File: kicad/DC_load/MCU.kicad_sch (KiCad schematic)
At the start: 125 parts, among them J1 BNC, J10 DC fan connector, J6 USB_B, J8 FT232 programming port, J9 Conn_01x04_Socket, Q1 MMBT5401, Q13 AO3400A, SW1 RotaryEncoder_Switch, SW2 RotaryEncoder_Switch, SW3 SW_Push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

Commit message: Added jumper.
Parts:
- added JP3: Jumper_2_Open, Jumper:SolderJumper-2_P1.3mm_Open_RoundedPad1.0x1.5mm, symbol Jumper:Jumper_2_Open
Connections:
- net CH1_CONTROL: now also JP3.2 (B)
- net at C22.2, R21.1, U1.3: now also JP3.1 (A)
- no-connect marks 16 -> 17
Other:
- note added: "Analog switch supply"
- note added: "Fan power supply"
- note added: "Inverter supply"
- note added: "MCU"
- note added: "Programming buttons"
- note added: "User input"
- note removed: "12 V fan 100 mArms"
- note removed: "MCU buttons"
- moved on the sheet: C16, C17, C18, C19, C21, C22, C23, C24, C25, C26, C27, C28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

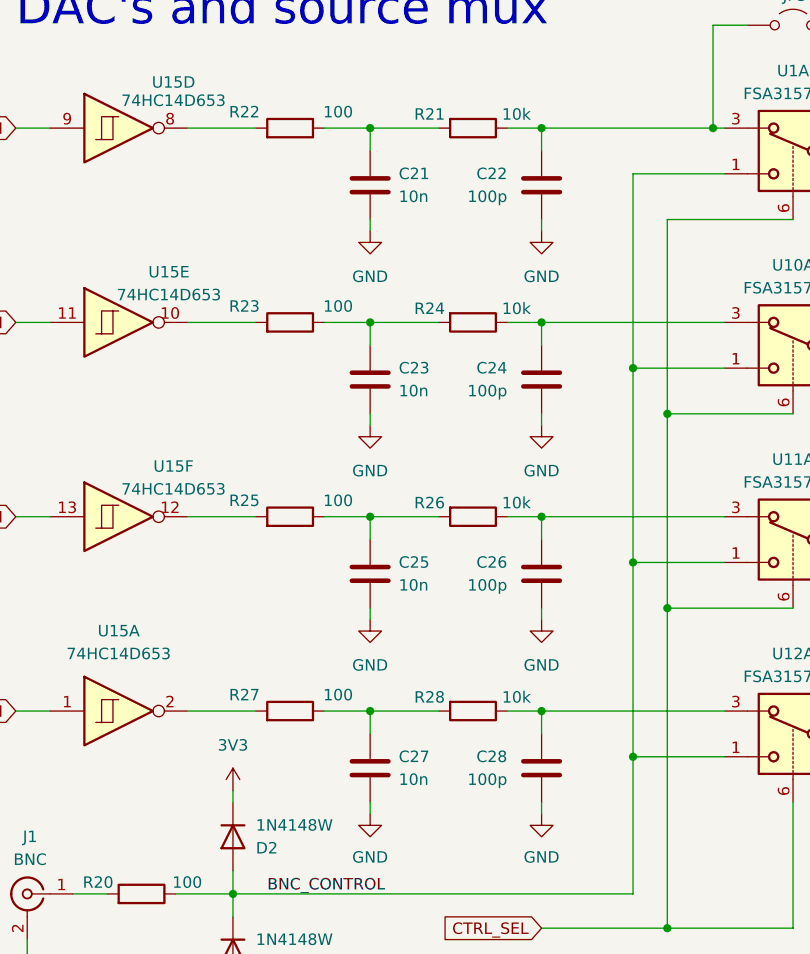
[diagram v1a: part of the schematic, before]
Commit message: More agresive PWM filtering.
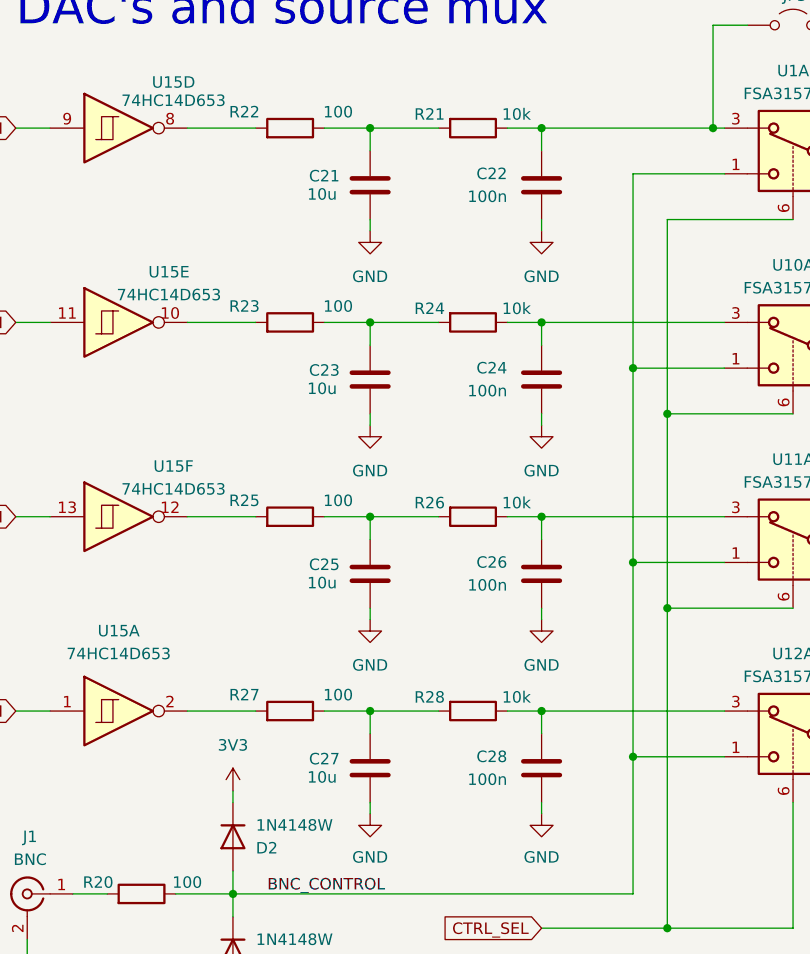
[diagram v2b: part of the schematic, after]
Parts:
- C21, C23, C25, C27: value 10n -> 10u; LCSC C57112 -> C96446
- C22, C24, C26, C28: value 100p -> 100n; LCSC C14858 -> C14663
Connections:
- net GND: now also C21.2, C23.2, C25.2, C27.2; no longer C21.1, C23.1, C25.1, C27.1
- net at R21.2, R22.1: now also C21.1; no longer C21.2
- net at R27.1, R28.2: now also C27.1; no longer C27.2
- net at R25.1, R26.2: now also C25.1; no longer C25.2
- net at R23.1, R24.2: now also C23.1; no longer C23.2

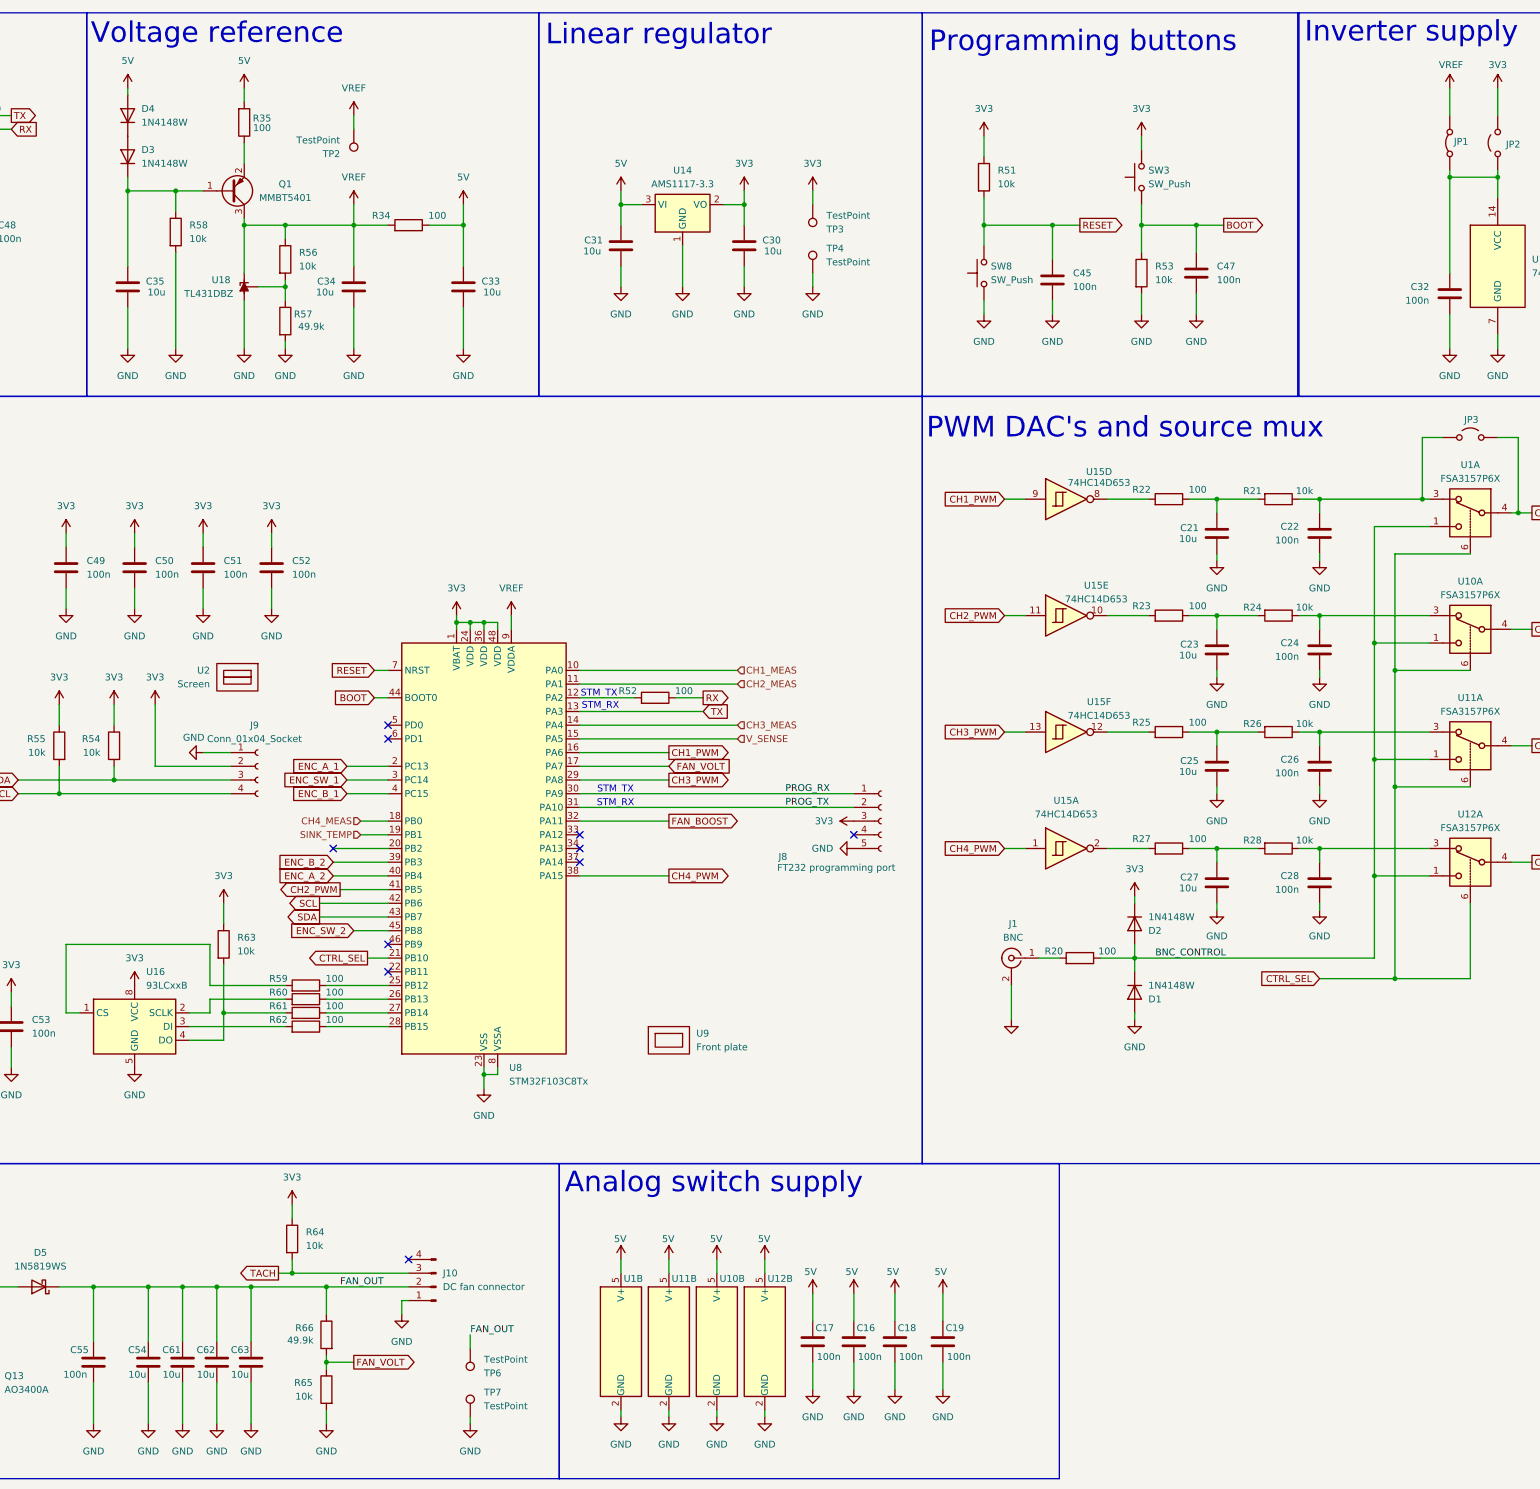
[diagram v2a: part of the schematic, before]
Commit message: Vbe multiplier, constant current source 12V mosfet gate driver. RC filters moved lower. INA181 for 20x gain, 50 mOhm shunts. Jumper moved to BNC. Rough placement initiated.
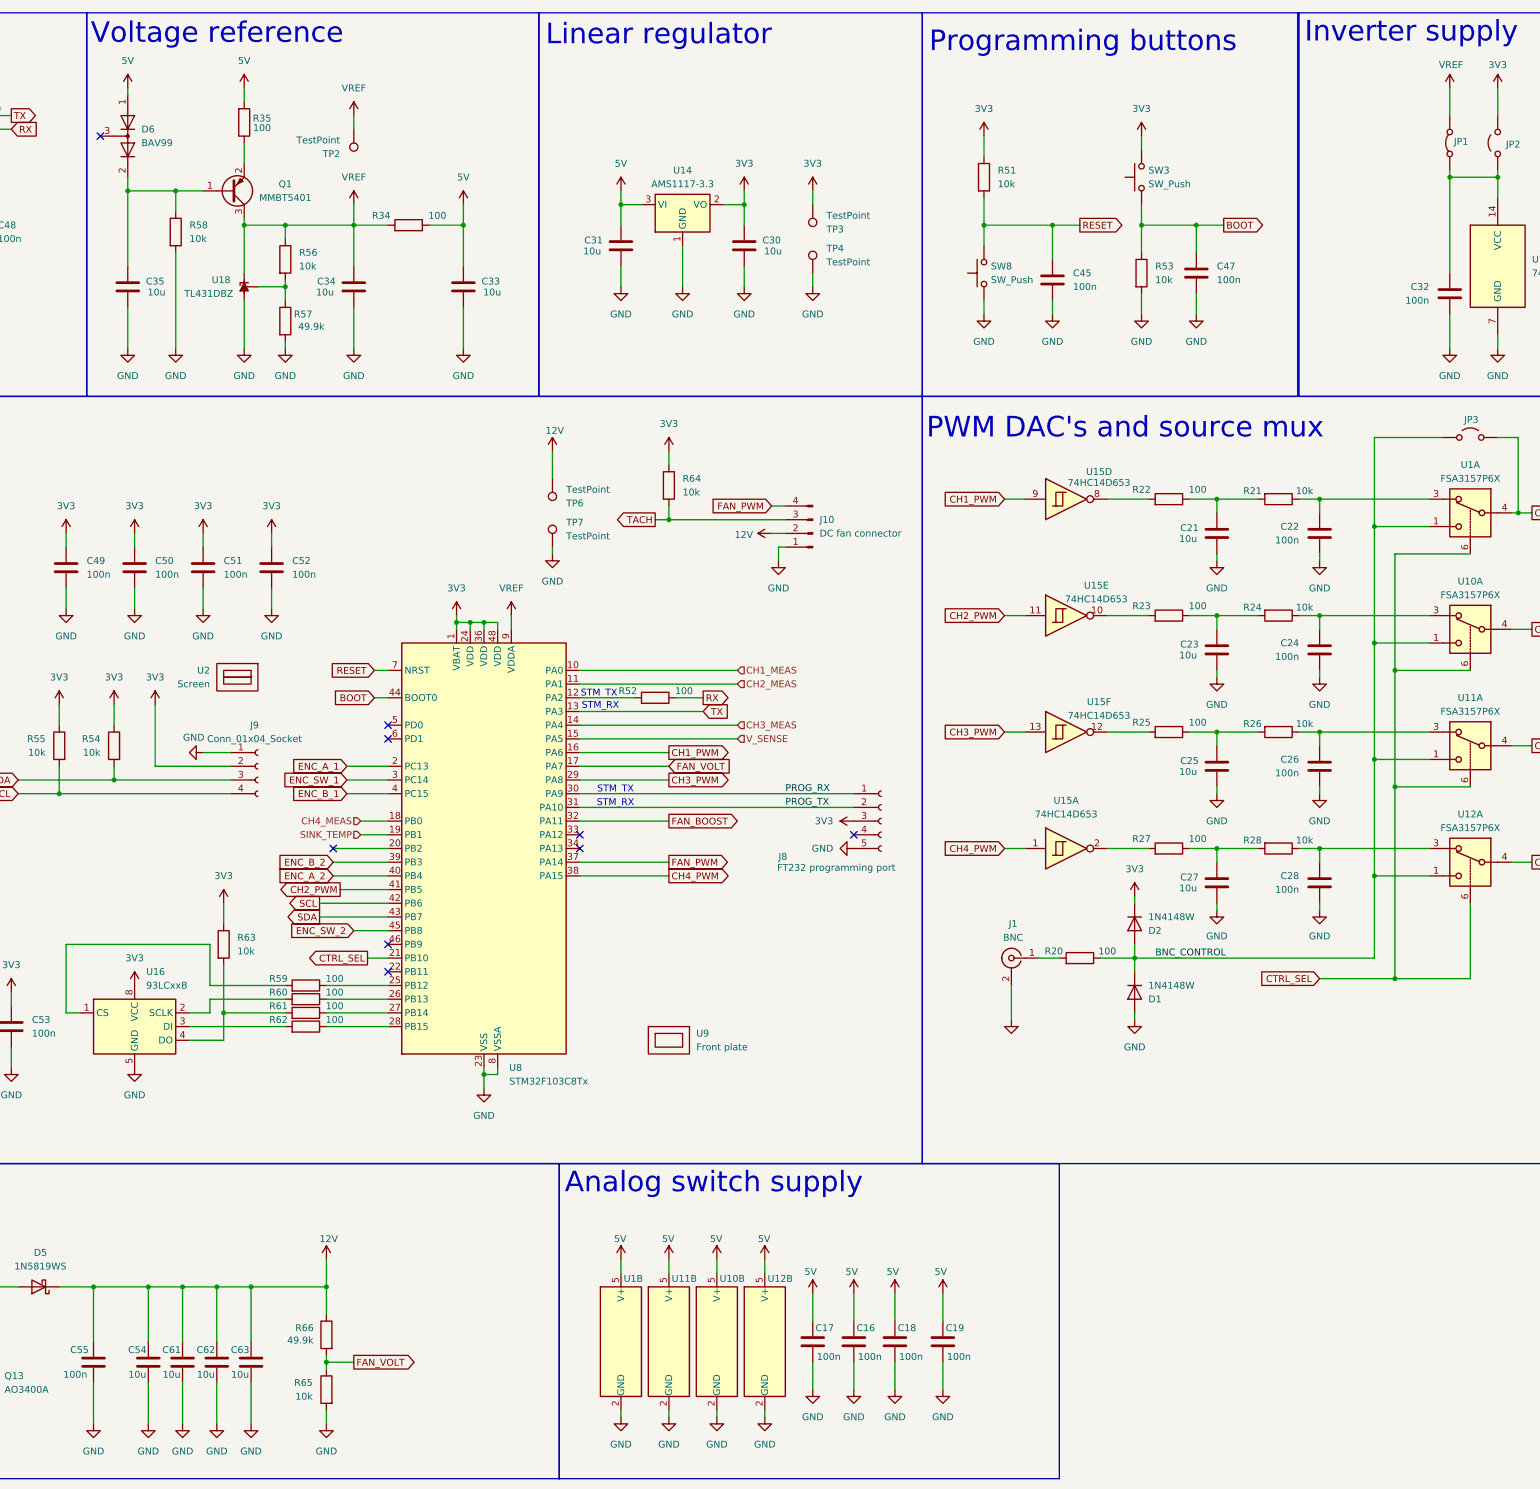
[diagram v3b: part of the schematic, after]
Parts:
- removed D3, D4: 1N4148W, Diode_SMD:D_SOD-123, symbol Diode:1N4148W
- added D6: BAV99, Package_TO_SOT_SMD:SOT-23, symbol Diode:BAV99
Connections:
- net 5V: now also D6.1 (K)
- net BNC_CONTROL: now also JP3.1 (A)
- net at C35.1, Q1.1 (B), R58.1: now also D6.2 (A)
- net at C22.2, R21.1, U1.3: no longer JP3.1 (A)
- net FAN_PWM: now reaches J10.4 (Pin_4)
- net FAN_PWM: now also U8.37 (PA14)
- net FAN_OUT renamed 12V
- no-connect marks 17 -> 16
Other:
- moved on the sheet: J10, R64, TP6, TP7

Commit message: Još gate driver layout.
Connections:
- no-connect marks 16 -> 17
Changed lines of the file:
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@@
+	)
+	(no_connect
+		(at 300.99 218.44)
 	)
 	(no_connect
